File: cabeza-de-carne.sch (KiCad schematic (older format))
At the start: 20 parts, among them J1 Stomp_Connector, J2 Power_Connector, Q1 2N3904, Q2 BC182L

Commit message: 0.2: more compact board
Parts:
- D1: footprint LED_THT:LED_D5.0mm -> LED_THT:LED_D3.0mm
- D2: footprint Diode_THT:D_DO-41_SOD81_P10.16mm_Horizontal -> diodes:DO41-2
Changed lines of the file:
@@
 F 0 "D2" H 1400 1184 50  0000 C CNN
 F 1 "1N5817" H 1400 1275 50  0000 C CNN
-F 2 "Diode_THT:D_DO-41_SOD81_P10.16mm_Horizontal" H 1400 1225 50  0001 C CNN
+F 2 "diodes:DO41-2" H 1400 1225 50  0001 C CNN
 F 3 "http://www.vishay.com/docs/88525/1n5817.pdf" H 1400 1400 50  0001 C CNN
 	1    1400 1400
@@
 F 0 "D1" H 1093 1965 50  0000 C CNN
 F 1 "LED" H 1093 1874 50  0000 C CNN
-F 2 "LED_THT:LED_D5.0mm" H 1100 1750 50  0001 C CNN
+F 2 "LED_THT:LED_D3.0mm" H 1100 1750 50  0001 C CNN
 F 3 "~" H 1100 1750 50  0001 C CNN
 	1    1100 1750

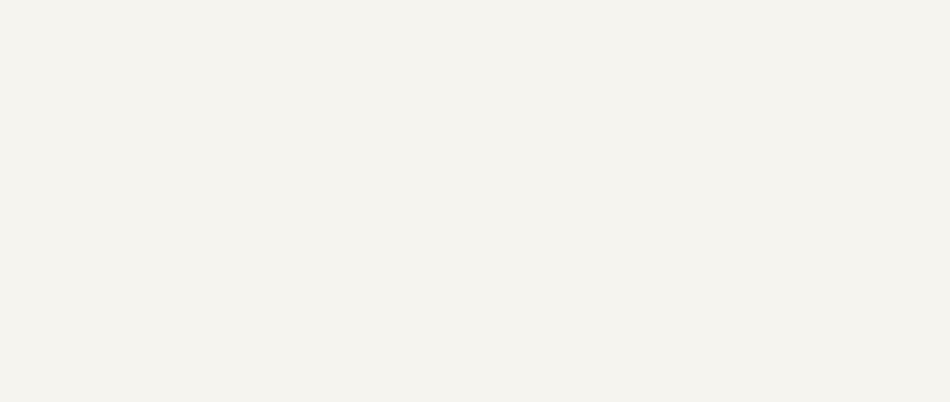
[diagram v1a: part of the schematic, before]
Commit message: v0.3: longer footprint for D1 (not standing anymore), fixed silkscreen for Q2 (had wrong markings for B,C)
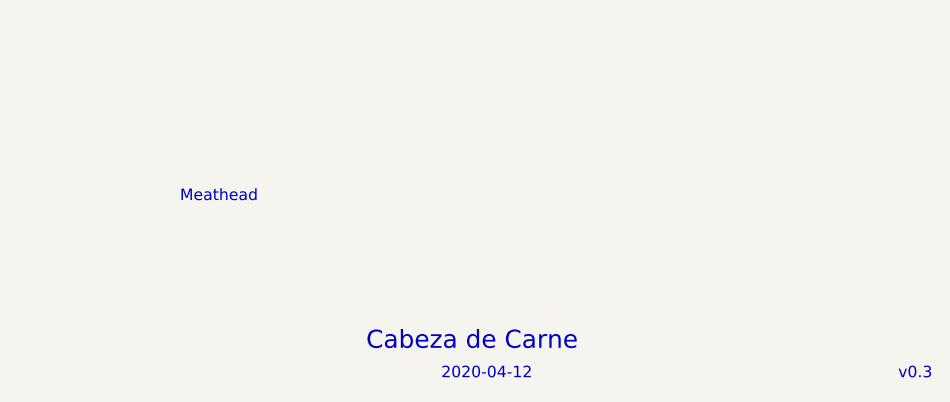
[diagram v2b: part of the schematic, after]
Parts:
- D2: footprint diodes:DO41-2 -> diodes:DO41-3
- Q2: footprint rockola_kicad_footprints:TO92_EBCE -> rockola_kicad_footprints:TO92_ECBE
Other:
- note added: "2020-04-12"
- note added: "Cabeza de Carne"
- note added: "Meathead"
- note added: "v0.3"
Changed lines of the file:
@@
 EESchema Schematic File Version 5
-EELAYER 32 0
+EELAYER 33 0
 EELAYER END
 $Descr A4 11693 8268
@@
 Wire Wire Line
 	4550 2100 4800 2100
+Text Notes 7925 6850 2    50   ~ 0
+Meathead
+Text Notes 9125 7625 2    50   ~ 0
+2020-04-12
+Text Notes 9325 7500 2    79   ~ 0
+Cabeza de Carne
+Text Notes 10875 7625 2    50   ~ 0
+v0.3
 Text GLabel 950  1750 0    50   Input ~ 0
 LED-
@@
 F 0 "D2" H 1400 1184 50  0000 C CNN
 F 1 "1N5817" H 1400 1275 50  0000 C CNN
-F 2 "diodes:DO41-2" H 1400 1225 50  0001 C CNN
+F 2 "diodes:DO41-3" H 1400 1225 50  0001 C CNN
 F 3 "http://www.vishay.com/docs/88525/1n5817.pdf" H 1400 1400 50  0001 C CNN
 	1    1400 1400
@@
 $EndComp
 $Comp
+L Device:CP C6
+U 1 1 5E785A25
+P 2100 1750
+F 0 "C6" H 2218 1795 50  0000 L CNN
+F 1 "47u" H 2218 1705 50  0000 L CNN
+F 2 "Capacitor_THT:CP_Radial_D5.0mm_P2.50mm" H 2138 1600 50  0001 C CNN
+F 3 "~" H 2100 1750 50  0001 C CNN
+	1    2100 1750
+	1    0    0    -1
+$EndComp
+$Comp
 L Device:C C1
 U 1 1 5E6D2E81
@@
 $EndComp
 $Comp
+L Device:CP C5
+U 1 1 5E6DAB4A
+P 3700 2650
+F 0 "C5" V 3954 2650 50  0000 C CNN
+F 1 "10u" V 3863 2650 50  0000 C CNN
+F 2 "Capacitor_THT:CP_Radial_D5.0mm_P2.50mm" H 3738 2500 50  0001 C CNN
+F 3 "~" H 3700 2650 50  0001 C CNN
+	1    3700 2650
+	0    -1   -1   0
+$EndComp
+$Comp
 L Device:C C4
 U 1 1 5E6D978B
@@
 F 3 "~" H 3850 1000 50  0001 C CNN
 	1    3850 1000
-	0    -1   -1   0
-$EndComp
-$Comp
-L Device:CP C6
-U 1 1 5E785A25
-P 2100 1750
-F 0 "C6" H 2218 1795 50  0000 L CNN
-F 1 "47u" H 2218 1705 50  0000 L CNN
-F 2 "Capacitor_THT:CP_Radial_D5.0mm_P2.50mm" H 2138 1600 50  0001 C CNN
-F 3 "~" H 2100 1750 50  0001 C CNN
-	1    2100 1750
-	1    0    0    -1
-$EndComp
-$Comp
-L Device:CP C5
-U 1 1 5E6DAB4A
-P 3700 2650
-F 0 "C5" V 3954 2650 50  0000 C CNN
-F 1 "10u" V 3863 2650 50  0000 C CNN
-F 2 "Capacitor_THT:CP_Radial_D5.0mm_P2.50mm" H 3738 2500 50  0001 C CNN
-F 3 "~" H 3700 2650 50  0001 C CNN
-	1    3700 2650
 	0    -1   -1   0
 $EndComp
@@
 F 0 "Q2" H 3541 2145 50  0000 L CNN
 F 1 "BC182L" H 3541 2055 50  0000 L CNN
-F 2 "rockola_kicad_footprints:TO92_EBCE" H 3550 2025 50  0001 L CIN
+F 2 "rockola_kicad_footprints:TO92_ECBE" H 3550 2025 50  0001 L CIN
 F 3 "http://www.b-kainka.de/Daten/Transistor/BC108.pdf" H 3350 2100 50  0001 L CNN
 	1    3350 2100
